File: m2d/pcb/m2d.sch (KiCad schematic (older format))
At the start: 0 parts

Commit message: make a good start on m2d schematic
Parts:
- added C? (x10): 10µ, 1411, symbol CP1
- added C? (x20): 100n, 0603, symbol C
- added C? (x3): 2µ2, 0603, symbol CP1
- added C?: 1n, 0603, symbol C
- added C? (x2): 15p, 0603, symbol C
- added C?: 1µ, 0805, symbol CP1
- added C?: 10n, 0603, symbol C
- added C?: 470n, 0603, symbol C
- added C?: 4µ7, 0603, symbol CP1
- added C?: 220n, 0603, symbol C
- added D?: RED, 0603, symbol LED
- added D? (x3): YELLOW, 0603, symbol LED
- added IC?: APU1205-HF-3, symbol APU1205-HF-3
- added IC?: ADXL375, symbol ADXL375
- added IC?: STM32F303C, symbol STM32F303C
- added IC?: MS5611-01BA03, symbol MS5611-01BA03
- added IC?: ADXL345, symbol ADXL345
- added IC? (x2): ADuM5201, symbol ADuM5201
- added IC?: HMC5883L, symbol HMC5883L
- added IC?: L3G4200D, symbol L3G4200D
- added IC?: AD8495, symbol AD8495
- added IC?: AD8226, 8MSOP, symbol AD8226
- added IC?: OP1177, 8MSOP, symbol OP1177
- added K?: CONN_3, symbol CONN_3
- added P? (x3): CONN_2, symbol CONN_2
- added P? (x2): CONN_4, symbol CONN_4
- added P?: SWD, symbol SWD
- added R? (x11): 10k, 0603, symbol R
- added R?: 1k, 0603, symbol R
- added R? (x7): 100, 0603, symbol R
- added R?: R, 0603, symbol R
- added R? (x3): 120, 0603, symbol R
- added TP? (x16): TESTPAD, symbol TESTPAD
- added U?: RG LED, symbol PART
- added U?: ARM SW, symbol PART
- added U?: BAT BOX, symbol PART
- added X?: 8M, HC49/S, symbol CRYSTAL
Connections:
- new net: C?.1, IC?.4 (CBYP)
- new net: P?.1 (P1), P?.2 (PM)
- new net: C?.1, R?.1, X?.2
- new net: C?.1, IC?.5 (PD0_OSCIN), X?.1
- new net: C?.1, C?.1, IC?.10 (VE2), IC?.16 (VISO), P?.1 (P1) (x2)
- new net: IC?.14 (OUT_A), P?.2 (P2) (x2)
- new net: IC?.13 (IN_B), P?.3 (P3) (x2)
- new net: C?.2, C?.2, IC?.11 (VSEL), IC?.15 (GNDISO), IC?.9 (GNDISO), P?.4 (P4) (x2)
- new net: P?.1 (P1), R?.1, R?.1
- new net: IC?.6 (PD1_OSCOUT), R?.2
- new net: D?.1 (A), R?.1 (x4)
- new net: C?.1, C?.2, IC?.1 (VDD1) (x2)
- new net: C?.1, IC?.10 (C1)
- new net: C?.2, IC?.12 (SETC)
- new net: C?.1, IC?.8 (SETP)
- new net: C?.2, C?.2, IC?.14 (PLLFILT)
- new net: IC?.1 (-IN), K?.2 (PM)
- new net: IC?.2 (RG), R?.1
- new net: IC?.3 (RG), R?.2
- new net: IC?.4 (+IN), R?.2, R?.2
- new net: IC?.2 (-IN), IC?.6 (OUT), IC?.6 (REF)
- new net: C?.1, R?.1
- new net: IC?.3 (+IN), R?.1, R?.2
- new net: K?.1 (P1), R?.1
- new net +BATT: C?.1, IC?.1 (VIN), IC?.3 (EN), P?.2 (PM), R?.1, TP?.1 (TP)
- new net BARO_CS: IC?.25 (PB12), IC?.4 (CSB), IC?.5 (CSB), R?.2, TP?.1 (TP)
- new net BARO_MISO: IC?.27 (PB14), IC?.6 (SDO), TP?.1 (TP)
- new net BARO_MOSI: IC?.28 (PB15), IC?.7 (SDI), TP?.1 (TP)
- new net BARO_SCK: IC?.26 (PB13), IC?.8 (SCLK), TP?.1 (TP)
- new net BAT_MON: C?.1, IC?.10 (PA0_WKUP), R?.1, R?.2, TP?.1 (TP)
- new net GND: C?.1, C?.1, C?.1, C?.1, C?.1, C?.1, C?.2, C?.2, C?.2, C?.2, C?.2, C?.2, C?.2, C?.2, C?.2, C?.2, C?.2, C?.2, C?.2, C?.2, C?.2, C?.2, C?.2, C?.2, C?.2, C?.2, C?.2, C?.2, C?.2, C?.2, C?.2, C?.2, C?.2, C?.2, C?.2, D?.2 (K), D?.2 (K), D?.2 (K), D?.2 (K), IC?.10 (GND), IC?.11 (GND), IC?.11 (GND), IC?.12 (GND), IC?.13 (GND), IC?.2 (GND), IC?.2 (GND), IC?.2 (GND), IC?.2 (GND1), IC?.2 (GND1), IC?.2 (PS), IC?.23 (GND2), IC?.3 (GND), IC?.35 (GND3), IC?.4 (GND), IC?.4 (GND), IC?.4 (Vs-), IC?.44 (BOOT0), IC?.47 (GND1), IC?.5 (-Vs), IC?.5 (GND), IC?.5 (GND), IC?.5 (RCIN), IC?.5 (RCIN), IC?.8 (GND), IC?.8 (GND1), IC?.8 (GND1), IC?.8 (GNDA), IC?.9 (GND), IC?.9 (GND), K?.3 (P3), P?.1 (P1), P?.3 (GND), P?.5 (GND), P?.9 (GND), R?.1, R?.2, R?.2, R?.2, TP?.1 (TP)
- new net GYRO_DRDY: IC?.6 (DRDY)
- new net GYRO_SCL: IC?.2 (SCLK), IC?.45 (PB8), R?.2
- new net GYRO_SDA: IC?.3 (SDI), IC?.46 (PB9), R?.2
- new net HG_ACCEL_CS: IC?.14 (PA4), IC?.7 (CS), R?.2, TP?.1 (TP)
- new net HG_ACCEL_INT1: IC?.8 (INT1)
- new net HG_ACCEL_INT2: IC?.9 (INT2)
- new net HG_ACCEL_MISO: IC?.12 (SDO), IC?.16 (PA6), TP?.1 (TP)
- new net HG_ACCEL_MOSI: IC?.13 (SDI), IC?.17 (PA7), TP?.1 (TP)
- new net HG_ACCEL_SCK: IC?.14 (SCLK), IC?.15 (PA5), TP?.1 (TP)
- new net LED_1: R?.2
- new net LED_2: R?.2
- new net LED_3: R?.2
- new net LED_A: R?.2, R?.2
- new net LED_C: P?.2 (PM)
- new net LG_ACCEL_CS: IC?.20 (PB2), IC?.7 (CS), R?.2
- new net LG_ACCEL_INT1: IC?.8 (INT1)
- new net LG_ACCEL_INT2: IC?.9 (INT2)
- new net LG_ACCEL_MISO: IC?.12 (SDO), IC?.40 (PB4)
- new net LG_ACCEL_MOSI: IC?.13 (SDI), IC?.41 (PB5)
- new net LG_ACCEL_SCK: IC?.14 (SCLK), IC?.39 (PB3)
- new net MAGNO_DRDY: IC?.15 (DRDY)
- new net MAGNO_SCL: IC?.1 (SCL), IC?.30 (PA9), R?.2, TP?.1 (TP)
- new net MAGNO_SDA: IC?.16 (SDA), IC?.31 (PA10), R?.2, TP?.1 (TP)
- new net SER_IN_1: IC?.4 (OUT_B), IC?.43 (PB7)
- new net SER_IN_2: IC?.13 (PA3), IC?.4 (OUT_B), TP?.1 (TP)
- new net SER_OUT_1: IC?.3 (IN_A), IC?.42 (PB6)
- new net SER_OUT_2: IC?.12 (PA2), IC?.3 (IN_A), TP?.1 (TP)
- new net STRAIN_1: IC?.7 (OUT)
- new net SWCLK: IC?.37 (PA14), P?.4 (SWDCLK/TCK)
- new net SWDIO: IC?.34 (PA13), P?.2 (SWDIO/TMS)
- new net VCC: C?.1, C?.1, C?.1, C?.1, C?.1, C?.1, C?.1, C?.1, C?.1, C?.1, C?.1, C?.1, C?.1, C?.1, C?.1, C?.1, C?.1, C?.1, C?.1, C?.1, C?.1, C?.2, C?.2, IC?.1 (VBAT), IC?.1 (VDD), IC?.1 (VDD_IO), IC?.1 (VDD_IO), IC?.1 (VDD_IO), IC?.13 (VDD_IO), IC?.15 (VDD), IC?.16 (VDD), IC?.2 (VDD), IC?.24 (VDD2), IC?.36 (VDD3), IC?.4 (VDD_IO), IC?.48 (VDD1), IC?.5 (CS), IC?.5 (VOUT), IC?.6 (RCSEL), IC?.6 (RCSEL), IC?.6 (Vs), IC?.6 (Vs), IC?.7 (VE1), IC?.7 (VE1), IC?.7 (Vs+), IC?.8 (+Vs), IC?.9 (VDDA), P?.1 (VTref), R?.1, R?.1, R?.1, R?.1, R?.1, R?.1, R?.1, R?.1, R?.1, R?.2, R?.2, TP?.1 (TP)
- new net nRST: C?.2, IC?.7 (NRST), P?.10 (nRESET)
- no-connect marks 0 -> 8
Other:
- note added: "BAROMETER"
- note added: "BATTERY MONITORING"
- note added: "EXTERNAL STATUS LED"
- note added: "GYROSCOPE"
- note added: "HIGH-G\nACCELEROMETER"
- note added: "INTERNAL STATUS LEDS"
- note added: "LOW-G\nACCELEROMETER"
- note added: "MAGNETOMETER"
- note added: "MICROCONTROLLER"
- note added: "POWER SUPPLY"
- note added: "SERIAL IN/OUT"
- note added: "SERIAL WIRE DEBUG"
- note added: "SPECIFY GAIN RESISTOR"
- note added: "STRAIN GAUGE 1"

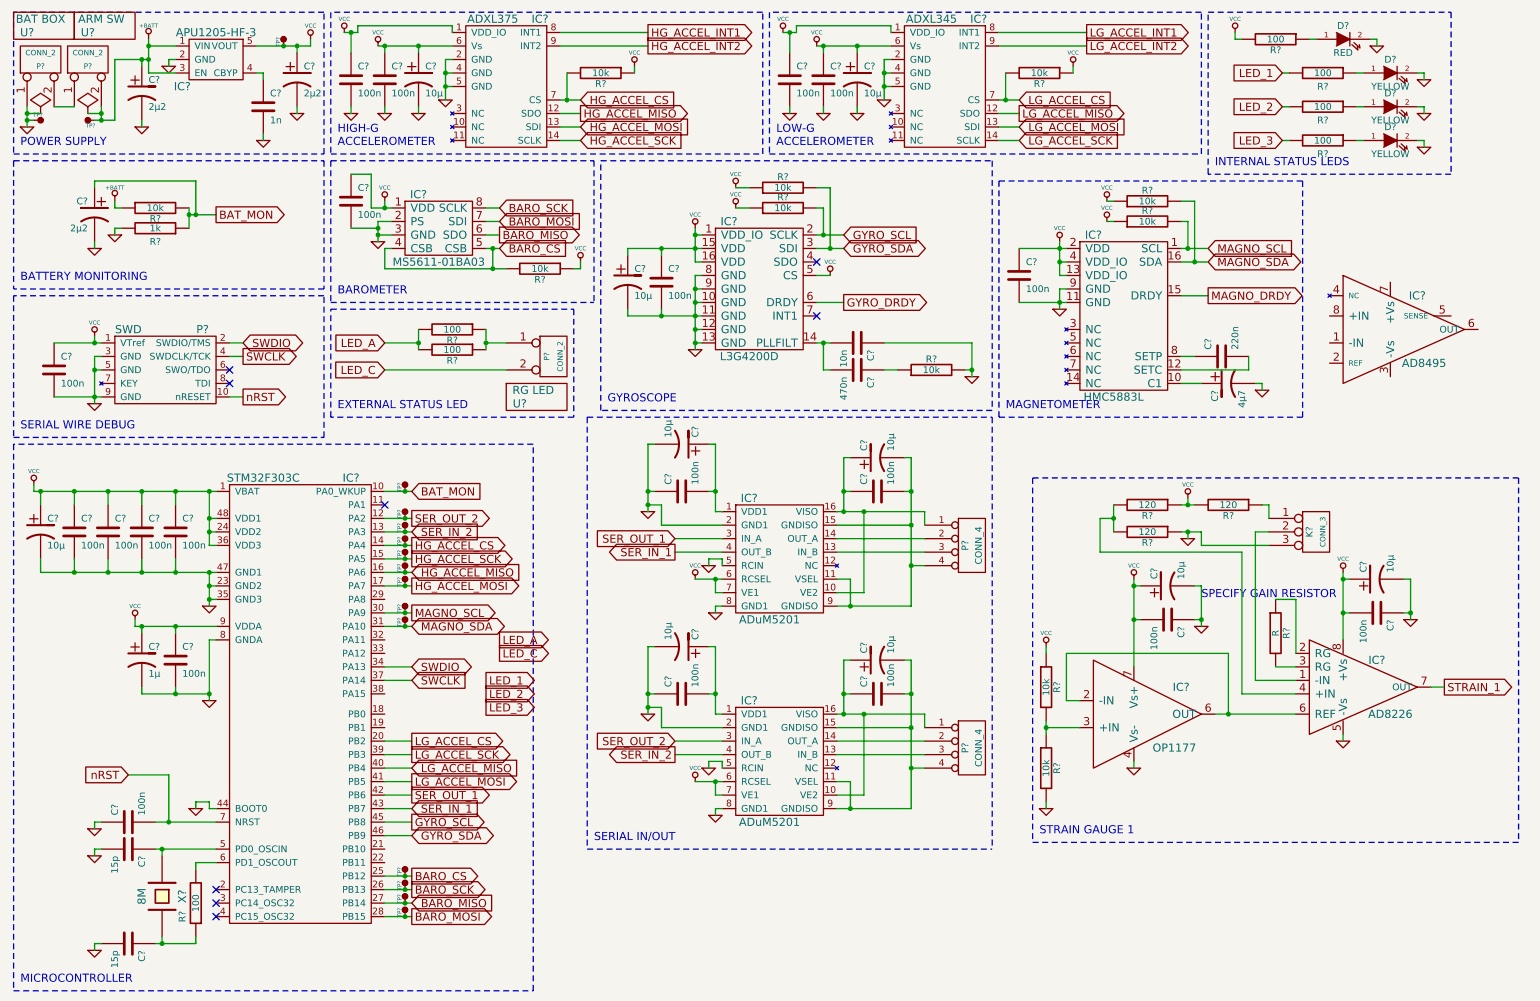
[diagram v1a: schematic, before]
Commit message: swap to f415, reorg sch into sheets, spec strain gauge Rg
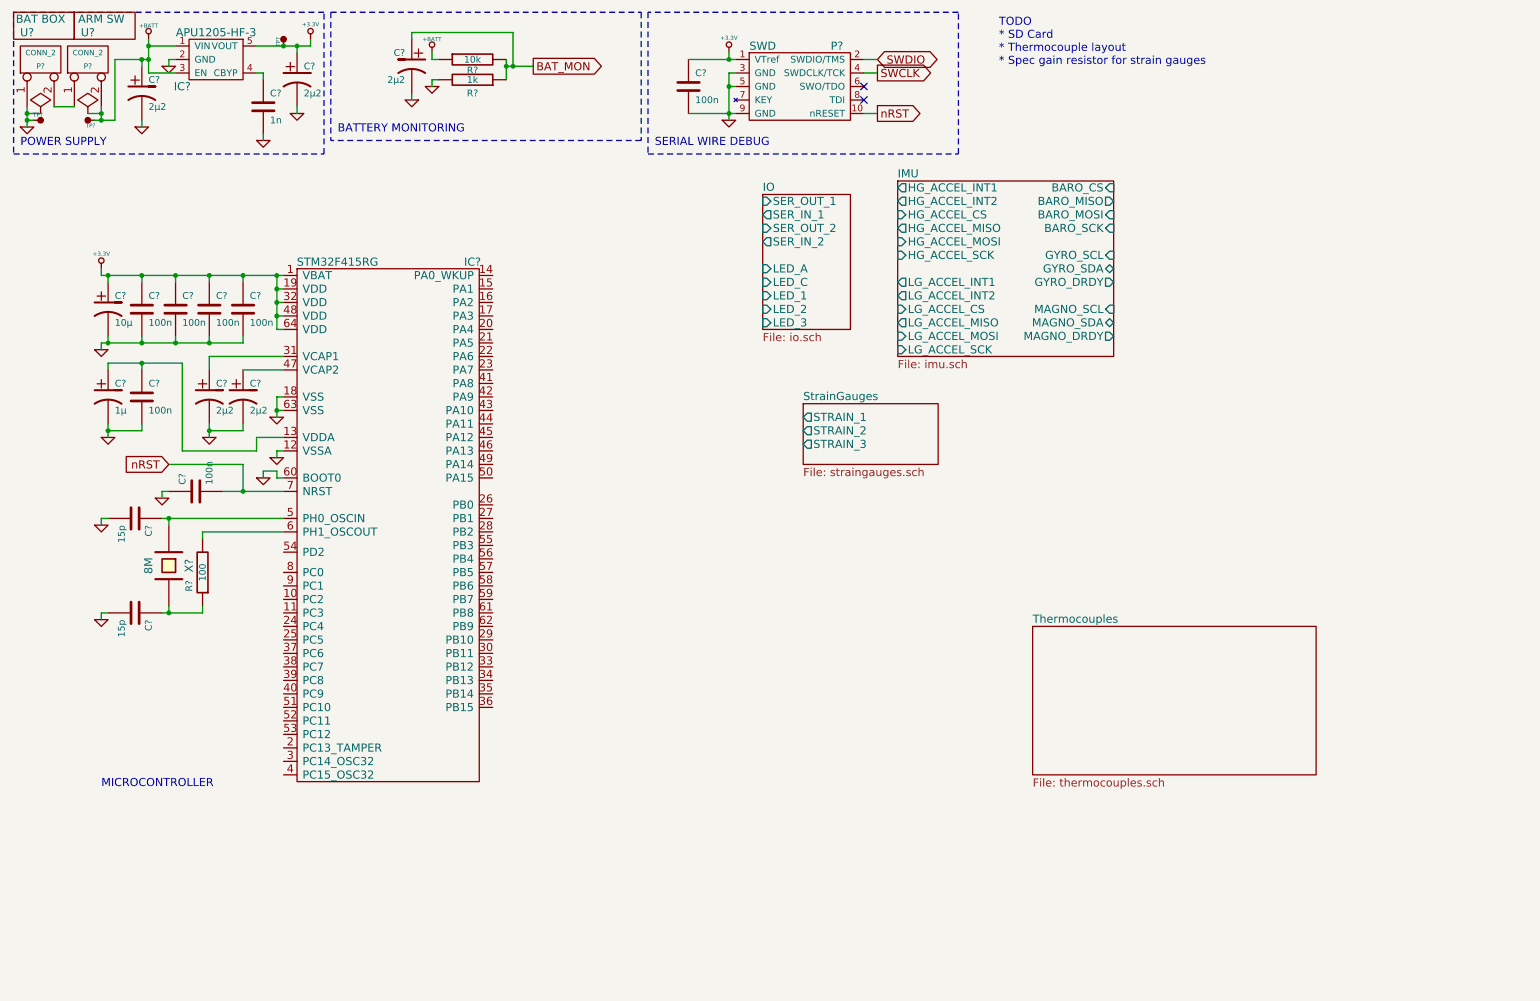
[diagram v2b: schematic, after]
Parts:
- removed C? (x9): 10µ, 1411, symbol CP1
- removed C? (x14): 100n, 0603, symbol C
- removed C?: 10n, 0603, symbol C
- removed C?: 470n, 0603, symbol C
- removed C?: 4µ7, 0603, symbol CP1
- removed C?: 220n, 0603, symbol C
- removed D?: RED, 0603, symbol LED
- removed D? (x3): YELLOW, 0603, symbol LED
- removed IC?: ADXL375, symbol ADXL375
- removed IC?: STM32F303C, symbol STM32F303C
- removed IC?: MS5611-01BA03, symbol MS5611-01BA03
- removed IC?: ADXL345, symbol ADXL345
- removed IC? (x2): ADuM5201, symbol ADuM5201
- removed IC?: HMC5883L, symbol HMC5883L
- removed IC?: L3G4200D, symbol L3G4200D
- removed IC?: AD8495, symbol AD8495
- removed IC?: AD8226, 8MSOP, symbol AD8226
- removed IC?: OP1177, 8MSOP, symbol OP1177
- removed K?: CONN_3, symbol CONN_3
- removed P? (x2): CONN_4, symbol CONN_4
- removed P?: CONN_2, symbol CONN_2
- removed P?: SWD, symbol SWD
- removed R? (x10): 10k, 0603, symbol R
- removed R? (x6): 100, 0603, symbol R
- removed R?: R, 0603, symbol R
- removed R? (x3): 120, 0603, symbol R
- removed TP? (x13): TESTPAD, symbol TESTPAD
- removed U?: RG LED, symbol PART
- added C? (x2): 2µ2, 0603, symbol CP1
- added C?: 100n, 0603, symbol C
- added IC?: STM32F415RG, symbol STM32F415RG
- added P?: SWD, symbol SWD
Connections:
- net GND: now also C?.2, C?.2, C?.2, IC?.12 (VSSA), IC?.18 (VSS), IC?.60 (BOOT0), IC?.63 (VSS), P?.3 (GND), P?.5 (GND), P?.9 (GND)
- net SWCLK: now also P?.4 (SWDCLK/TCK)
- net SWDIO: now also P?.2 (SWDIO/TMS)
- net nRST: now also IC?.7 (NRST), P?.10 (nRESET)
- net at C?.1, X?.1: now also IC?.5 (PH0_OSCIN)
- net at R?.2: now also IC?.6 (PH1_OSCOUT)
- net VCC renamed +3.3V
- net +3.3V: now also C?.1, IC?.1 (VBAT), IC?.19 (VDD), IC?.32 (VDD), IC?.48 (VDD), IC?.64 (VDD), P?.1 (VTref); no longer C?.1, C?.1
- new net: C?.1, C?.1, IC?.13 (VDDA)
- new net: C?.1, IC?.31 (VCAP1)
- new net: C?.1, IC?.47 (VCAP2)
- no-connect marks 8 -> 2
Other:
- note added: "TODO\n* SD Card\n* Thermocouple layout\n* Spec gain resistor for strain gauges"
- note removed: "BAROMETER"
- note removed: "EXTERNAL STATUS LED"
- note removed: "GYROSCOPE"
- note removed: "HIGH-G\nACCELEROMETER"
- note removed: "INTERNAL STATUS LEDS"
- note removed: "LOW-G\nACCELEROMETER"
- note removed: "MAGNETOMETER"
- note removed: "SERIAL IN/OUT"
- note removed: "SPECIFY GAIN RESISTOR"
- note removed: "STRAIN GAUGE 1"
- moved on the sheet: C?, R?, X?
